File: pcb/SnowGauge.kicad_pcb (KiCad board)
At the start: 2 copper layers, 80 x 62 mm, 27 parts, among them J1 BATTERY L91x4, J2 TFmini R/B/G/W, J3 I2C SPARE, Q1 2SJ334, Q2 2SK4017, Q3 2SK4017, U1 NJU7223F33, U2 NJU7223F50

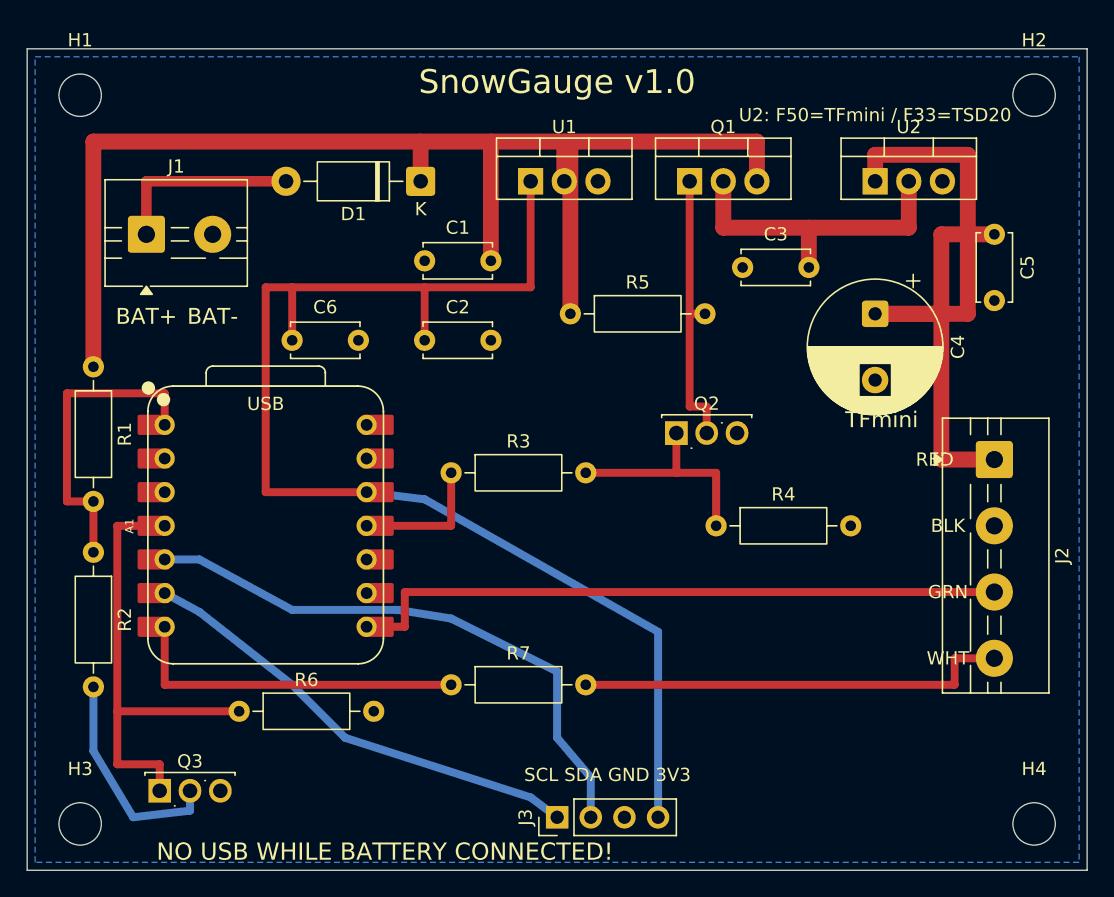
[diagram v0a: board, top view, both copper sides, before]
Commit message: Compact PCB v1.1: 64x50mm (35% smaller), fits BCAP091208G; DRC clean
Co-Authored-By: Claude Fable 5 <noreply@anthropic.com>
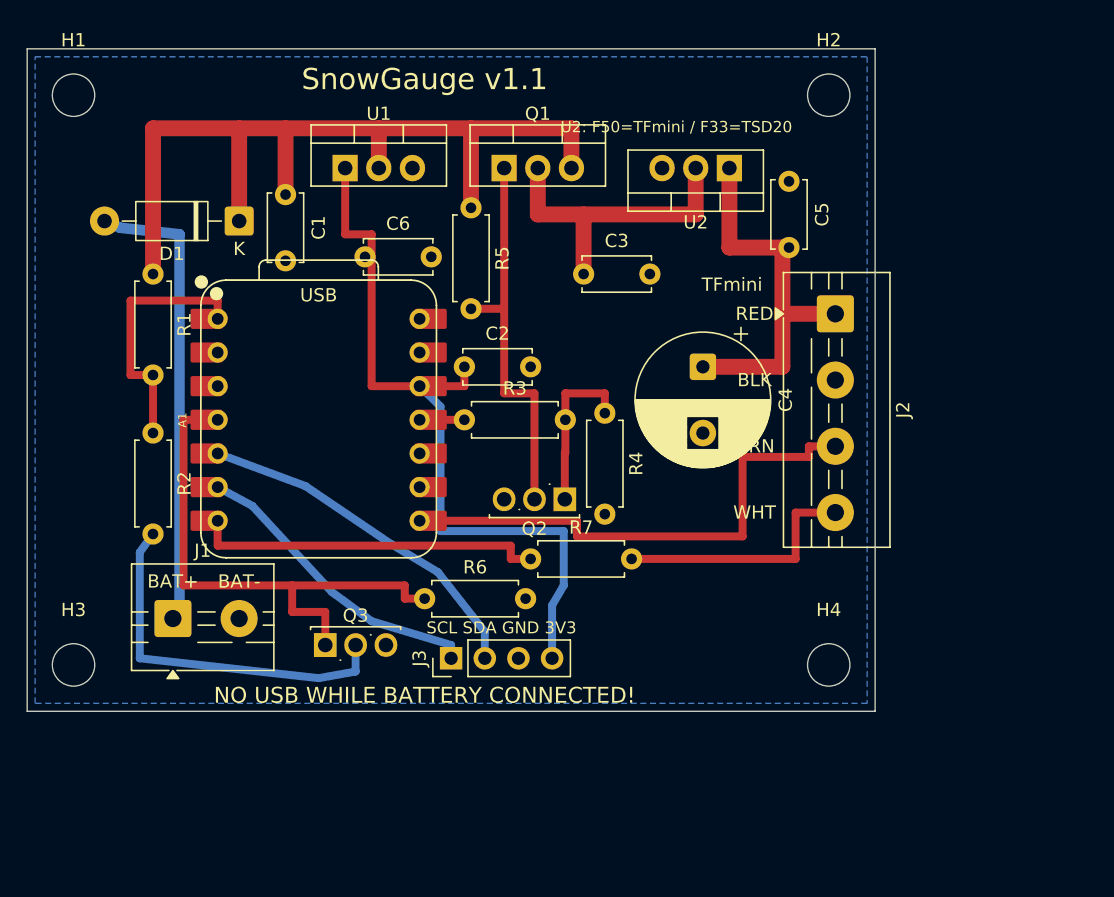
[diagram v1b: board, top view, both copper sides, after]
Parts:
- R1, R2, R3, R4, R5, R6, R7: footprint R_Axial_DIN0207_L6.3mm_D2.5mm_P10.16mm_Horizontal -> R_Axial_DIN0207_L6.3mm_D2.5mm_P7.62mm_Horizontal
- moved J1 29.1 mm to (31.0, 59.0)
- moved H4 19.6 mm to (80.5, 62.5)
- moved Q3 16.7 mm to (42.5, 61.0)
- moved R6 16.4 mm to (50.0, 57.5)
- moved J2 16.3 mm to (81.0, 36.0)
- moved C5 16.0 mm to (77.5, 26.0)
- moved H2 15.5 mm to (80.5, 19.5)
- moved J3 14.4 mm to (52.0, 62.0)
- moved Q1 14.0 mm to (56.0, 25.0)
- moved U1 14.0 mm to (44.0, 25.0)
- moved D1 14.0 mm to (36.0, 29.0)
- moved C4 13.6 mm to (71.0, 40.0)
- moved C3 12.0 mm to (62.0, 33.0)
- moved H3 12.0 mm to (23.5, 62.5)
- moved R4 12.0 mm to (63.6, 43.5), turned to -90 degrees
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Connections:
- C1 pad 1: GND -> VBAT
- C1 pad 2: VBAT -> GND
- C3 pad 1: GND -> VBAT_SW
- C3 pad 2: VBAT_SW -> GND
- C5 pad 1: 5V_SENS -> GND
- C5 pad 2: GND -> 5V_SENS
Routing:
- net 3V3_SYS: track 97.8 -> 58.2 mm
- net VBAT: track 98.1 -> 66.6 mm
- net 5V_SENS: track 58.0 -> 29.5 mm
- net BATP_RAW: track 14.5 -> 34.9 mm
- net I2C_SDA: track 43.5 -> 26.7 mm
- net TFMINI_RX: track 32.8 -> 18.9 mm
- net I2C_SCL: track 34.7 -> 22.8 mm
- net MEAS_LO: track 16.5 -> 28.1 mm
- net UART_RX: track 50.0 -> 39.4 mm
- net Q1_GATE: track 21.5 -> 29.8 mm
- net SENSOR_EN: track 10.4 -> 3.38 mm
- net VBAT_MEAS_EN: track 36.0 -> 41.3 mm
- net Q2_G: track 16.8 -> 12.5 mm
- net ADC_NODE: track 23.8 -> 19.7 mm
- net VBAT_SW: track 24.0 -> 23.4 mm
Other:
- board size 80 x 62 mm -> 64 x 50 mm
- board text added: "SnowGauge v1.1"
- board text removed: "SnowGauge v1.0"

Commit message: PCB v1.2: divider fed from VBAT_SW (fix ADC overvoltage, drop Q3/R6/D3), clear USB corridor, silk fixes; add breadboard wiring guide
Co-Authored-By: Claude Fable 5 <noreply@anthropic.com>
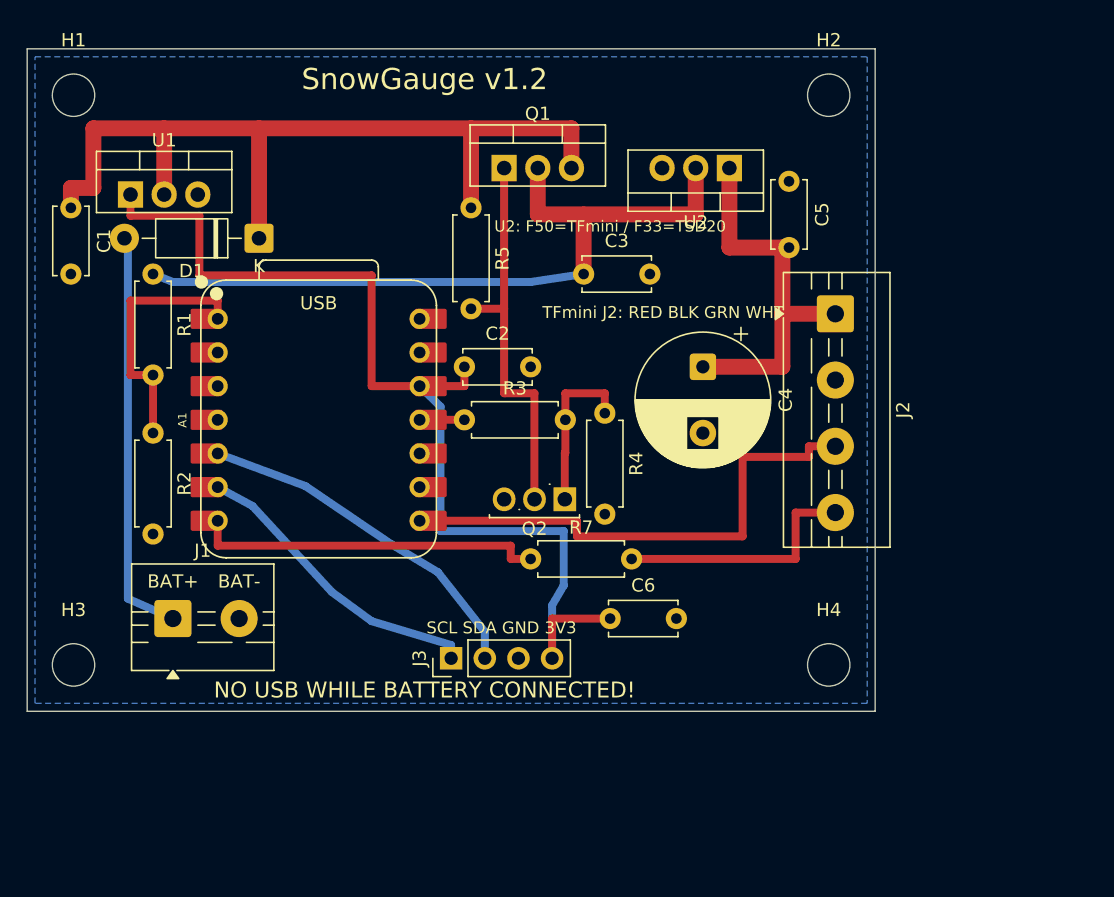
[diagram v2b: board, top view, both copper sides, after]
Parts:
- removed Q3: 2SK4017, TO-251-3_Vertical
- removed R6: 100k, R_Axial_DIN0207_L6.3mm_D2.5mm_P7.62mm_Horizontal
- moved C6 33.0 mm to (64.0, 59.0)
- moved U1 16.3 mm to (27.8, 27.0)
- moved C1 16.2 mm to (23.3, 28.0)
- moved D1 1.98 mm to (37.5, 30.3)
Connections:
- A1 pad 4: VBAT_MEAS_EN -> (no net)
- R1 pad 1: VBAT -> VBAT_SW
- R2 pad 2: MEAS_LO -> GND
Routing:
- net VBAT_MEAS_EN: track 41.3 -> 0.00 mm
- net VBAT_SW: track 23.4 -> 56.1 mm
- net MEAS_LO: track 28.1 -> 0.00 mm
- net 3V3_SYS: track 58.2 -> 79.2 mm
- net BATP_RAW: track 34.9 -> 31.6 mm
- net VBAT: track 66.6 -> 66.1 mm
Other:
- board text added: "SnowGauge v1.2"
- board text added: "TFmini J2: RED BLK GRN WHT"
- board text removed: "BLK"
- board text removed: "GRN"
- board text removed: "RED"
- board text removed: "SnowGauge v1.1"
- board text removed: "TFmini"
- board text removed: "WHT"

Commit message: PCB v1.2: terminals -> 3x 5.08mm 2P blocks (J1/J2/J4), silk adjustments
Co-Authored-By: Claude Fable 5 <noreply@anthropic.com>
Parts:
- added J4: TFmini GRN/WHT, TerminalBlock_Phoenix_MKDS-1,5-2-5.08_1x02_P5.08mm_Horizontal, F.Cu at (82.0, 48.0)
- J1: footprint TerminalBlock_MaiXu_MX126-5.0-02P_1x02_P5.00mm -> TerminalBlock_Phoenix_MKDS-1,5-2-5.08_1x02_P5.08mm_Horizontal
- J2: value TFmini R/B/G/W -> TFmini RED/BLK; footprint TerminalBlock_MaiXu_MX126-5.0-04P_1x04_P5.00mm -> TerminalBlock_Phoenix_MKDS-1,5-2-5.08_1x02_P5.08mm_Horizontal
- moved J1 1.50 mm to (31.0, 60.5)
- moved J2 1.00 mm to (82.0, 36.0)
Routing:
- net BATP_RAW: track 31.6 -> 32.8 mm
- net TFMINI_RX: track 18.9 -> 17.8 mm
- net UART_RX: track 39.4 -> 38.4 mm
- net 5V_SENS: track 29.5 -> 30.5 mm
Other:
- board text added: "+"
- board text added: "-"
- board text added: "GRN,WHT"
- board text added: "RED,BLK"
- board text removed: "BAT+"
- board text removed: "BAT-"
- board text removed: "TFmini J2: RED BLK GRN WHT"

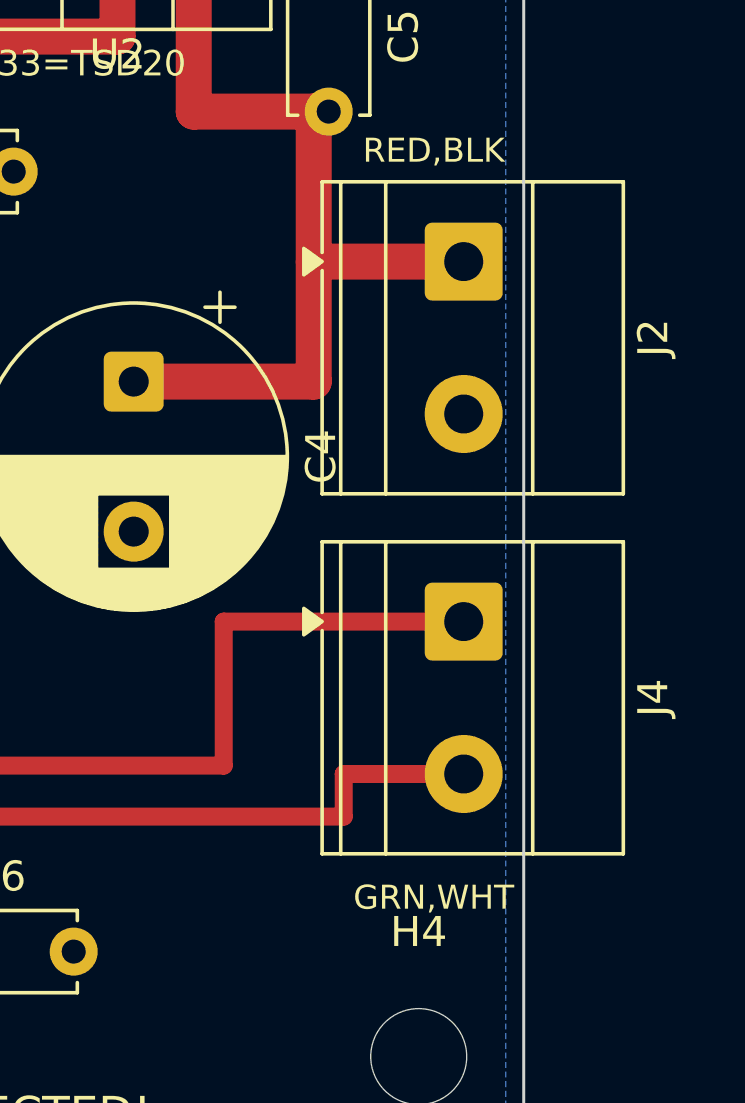
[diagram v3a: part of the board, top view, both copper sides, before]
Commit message: PCB v1.2: TFmini terminals as contiguous 4P footprint for interlocked 2Px2 blocks
Co-Authored-By: Claude Fable 5 <noreply@anthropic.com>
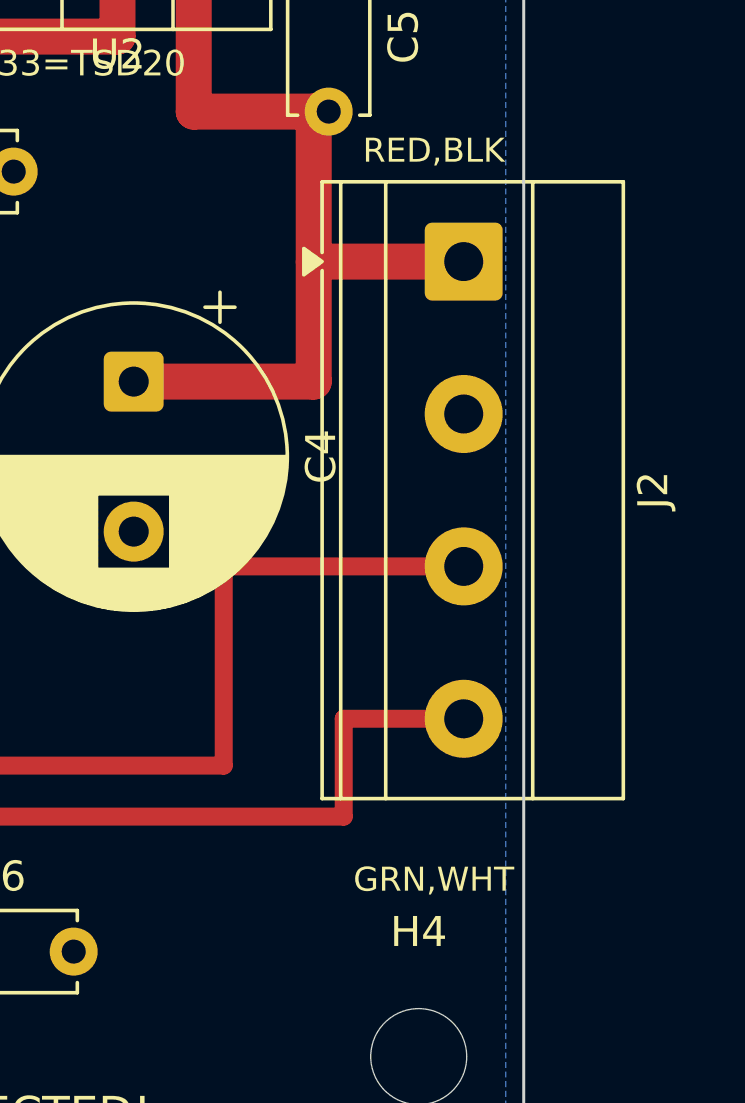
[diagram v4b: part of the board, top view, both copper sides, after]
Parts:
- removed J4: TFmini GRN/WHT, TerminalBlock_Phoenix_MKDS-1,5-2-5.08_1x02_P5.08mm_Horizontal
- J2: value TFmini RED/BLK -> TFmini 2Px2; footprint TerminalBlock_Phoenix_MKDS-1,5-2-5.08_1x02_P5.08mm_Horizontal -> TerminalBlock_Phoenix_MKDS-1,5-4-5.08_1x04_P5.08mm_Horizontal
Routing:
- net UART_RX: track 38.4 -> 40.2 mm
- net TFMINI_RX: track 17.8 -> 19.6 mm
